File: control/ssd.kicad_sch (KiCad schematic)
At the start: 3 parts, among them J1 Bus_M.2_Socket_M

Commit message: Cleanup/organization
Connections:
- net +3.3V renamed +3V3
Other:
- moved on the sheet: D1, J1, R1

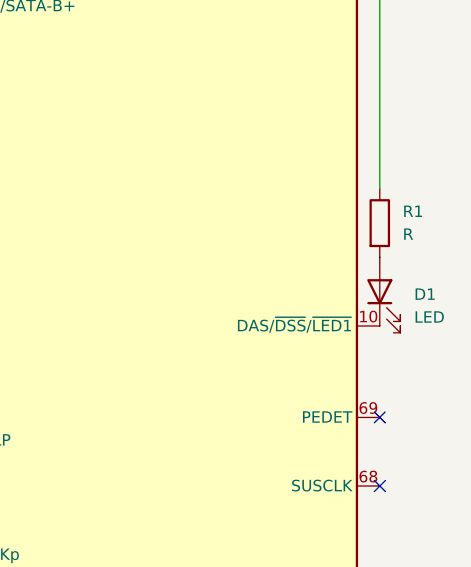
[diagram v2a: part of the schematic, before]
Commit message: Daughterboard setup, labeling, and testpoints
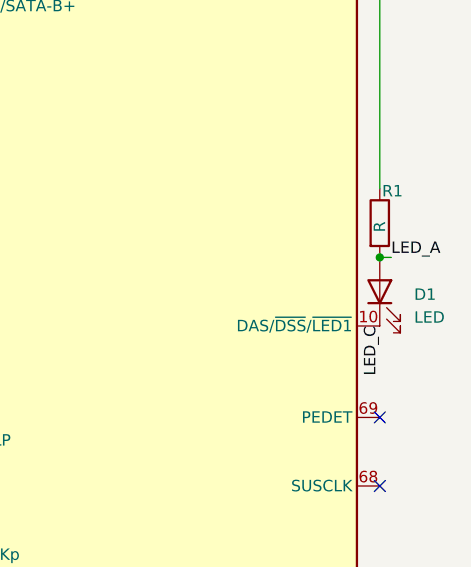
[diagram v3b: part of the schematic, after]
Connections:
- net LED_C: now reaches D1.1 (K), J1.10 (DAS/~{DSS}/~{LED1})
- net LED_A: now reaches D1.2 (A), R1.2
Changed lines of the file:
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@@
 		(color 0 0 0 0)
 	)
+	(junction
+		(at 163.83 97.79)
+		(diameter 0)
+		(color 0 0 0 0)
+	)
 	(no_connect
 		(at 113.03 74.93)
@@
 	(no_connect
 		(at 163.83 123.19)
+	)
+	(wire
+		(pts
+			(xy 165.1 97.79) (xy 163.83 97.79)
+		)
+		(stroke
+			(width 0)
+			(type default)
+		)
 	)
 	(wire
@@
 			(width 0)
 			(type default)
+		)
+	)
+	(label "LED_C"
+		(at 163.83 105.41 270)
+		(fields_autoplaced yes)
+		(effects
+			(font
+				(size 1.27 1.27)
+			)
+			(justify right bottom)
+		)
+	)
+	(label "LED_A"
+		(at 165.1 97.79 0)
+		(fields_autoplaced yes)
+		(effects
+			(font
+				(size 1.27 1.27)
+			)
+			(justify left bottom)
 		)
 	)
@@
 		(on_board yes)
 		(dnp no)
-		(fields_autoplaced yes)
 		(property "Reference" "R1"
-			(at 166.37 92.7099 0)
+			(at 164.084 90.424 0)
 			(effects
 				(font
@@
 		)
 		(property "Value" "R"
-			(at 166.37 95.2499 0)
-			(effects
-				(font
+			(at 163.83 94.996 90)
+			(effects
+				(font
